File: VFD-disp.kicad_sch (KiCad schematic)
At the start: 97 parts, among them J1 USB_C_Receptacle_USB2.0_14P, J2 Conn_02x03_Odd_Even, J3 Jack-DC, J4 Conn_02x03_Odd_Even, J5 Conn_02x03_Odd_Even, J6 Conn_02x03_Odd_Even, Q1 NMOS, Q3 NMOS, SW1 SW_SPST, U1 ESP32-C6-WROOM-1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

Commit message: Reroute pcb
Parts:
- removed F3: Fuse, Fuse:Fuse_0805_2012Metric, symbol Device:Fuse
- removed J3: Jack-DC, Connector_BarrelJack:BarrelJack_Horizontal, symbol Connector:Jack-DC
- removed Q1, Q3: NMOS, Package_TO_SOT_SMD:TO-252-2, symbol Simulation_SPICE:NMOS
- added Q1, Q2: Q_NMOS_GDS, Package_TO_SOT_SMD:TO-263-2, symbol Transistor_FET:Q_NMOS_GDS
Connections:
- net GND: now also Q2.3 (S)
- net at R10.2, R11.1: now also Q2.1 (G)
- net at R4.1, U6.8 (CS): now also Q1.3 (S)
- net at D1.2 (A), L1.2: now also Q1.2 (D)
- net at U6.1 (EXT): now also Q1.1 (G)
- net at IVLM3-5/1.22 (F2): now also Q2.2 (D)

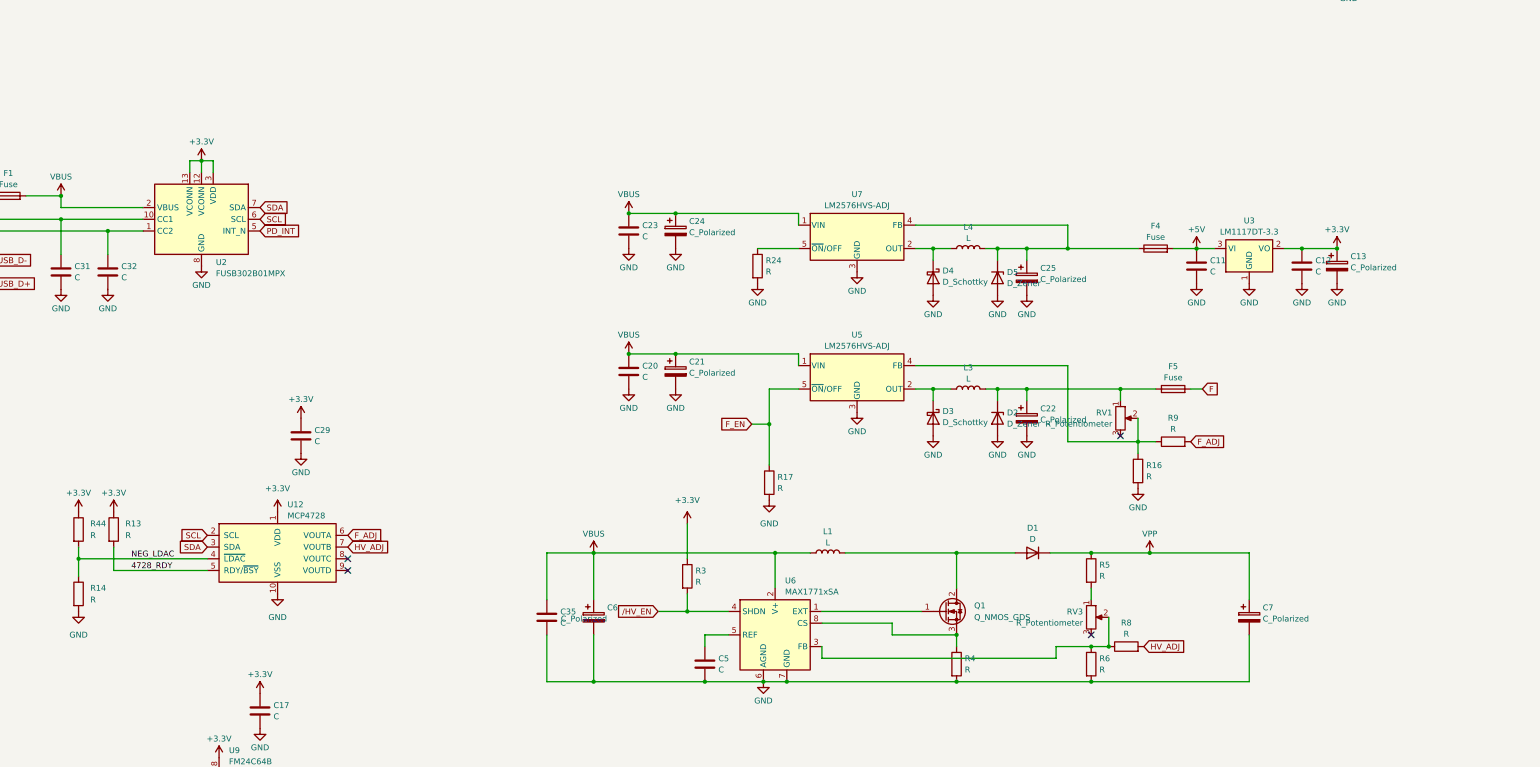
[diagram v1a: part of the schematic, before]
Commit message: Add chonky cermaics caps to be safe...
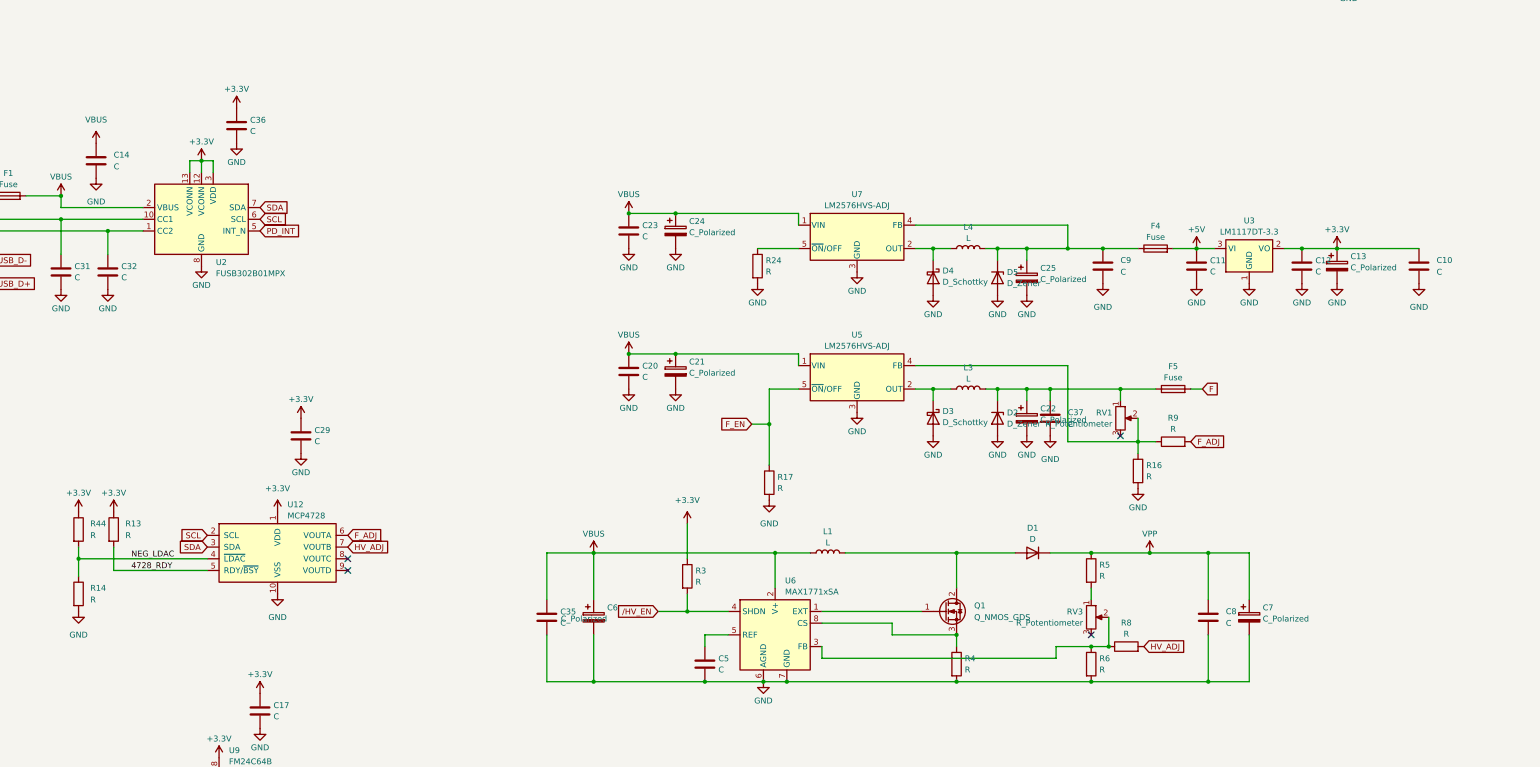
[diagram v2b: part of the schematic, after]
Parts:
- added C10, C14, C37, C8, C9: C, Capacitor_SMD:C_2220_5750Metric, symbol Device:C
- added C36: C, Capacitor_SMD:C_0805_2012Metric, symbol Device:C
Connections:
- net +3.3V: now also C10.1, C36.1
- net GND: now also C10.2, C14.2, C36.2, C37.2, C8.2, C9.2
- net VBUS: now also C14.1
- net VPP: now also C8.1
- net at C22.1, D2.1 (K), F5.1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: now also C37.1
- net at C25.1, D5.1 (K), F4.1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: now also C9.1

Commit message: Finish pcb
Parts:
- removed D5: D_Zener, Diode_SMD:D_MELF, symbol Device:D_Zener
- added C38, C39: 10uF, Capacitor_SMD:C_1206_3216Metric, symbol Device:C
- added C40, C41: C, Capacitor_SMD:C_0805_2012Metric, symbol Device:C
- added D6: BZV55B7V5, Diode_SMD:D_MiniMELF, symbol Diode:BZV55B7V5
- added Q3: Q_NPN_BEC, Package_TO_SOT_SMD:SOT-23, symbol Transistor_BJT:Q_NPN_BEC
- added R23, R27, R28, R29, R30: R, Resistor_SMD:R_0805_2012Metric, symbol Device:R
- added U13: TPS2116DRL, Package_TO_SOT_SMD:SOT-583-8, symbol Power_Management:TPS2116DRL
- added U14: KF50BDT, Package_TO_SOT_SMD:TO-252-2, symbol Regulator_Linear:KF50BDT
- added U8: USBLC6-2P6, Package_TO_SOT_SMD:SOT-666, symbol Power_Protection:USBLC6-2P6
- D1, D2, D3, D4: footprint Diode_SMD:D_MELF -> Diode_SMD:D_SMB
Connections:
- net +3.3V: now also R28.1, U8.5 (VBUS)
- net GND: now also C38.2, C39.2, C40.2, C41.2, Q3.2 (E), R27.2, R29.2, U13.1 (GND), U14.2 (GND), U8.2 (GND); no longer R24.2
- net USB_D+: now also U8.1 (I/O1); no longer U1.14 (GPIO13/USB_D+)
- net USB_D-: now also U8.3 (I/O2); no longer U1.13 (GPIO12/USB_D-)
- net VBUS: now also R24.1, C38.1, C40.1, R30.1, U14.1 (VI)
- net at C25.1, C9.1, L4.2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: now also R23.1, U13.3 (VIN1), U13.5 (MODE); no longer F4.1
- net at U7.5 (~{ON}/OFF): now also Q3.3 (C), R30.2; no longer R24.1
- net VBUS_ABOVE_TRESHOLD: now reaches U1.7 (MTDO/GPIO7)
- net VBUS_ABOVE_TRESHOLD: now also R28.2, U13.8 (ST)
- new net: C39.1, C41.1, U13.6 (VIN2), U14.3 (VO)
- new net: D6.2 (A), Q3.1 (B), R29.1
- new net: F4.1, U13.2 (VOUT), U13.7 (VOUT)
- new net: R23.2, R27.1, U13.4 (PR1)
- new net: D6.1 (K), R24.2
- new net PRE_USB_D+: U1.14 (GPIO13/USB_D+), U8.6 (I/O1)
- new net PRE_USB_D-: U1.13 (GPIO12/USB_D-), U8.4 (I/O2)
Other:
- moved on the sheet: C10, C11, C12, C13, C20, C21, C22, C35, C37, C5, C6, C7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

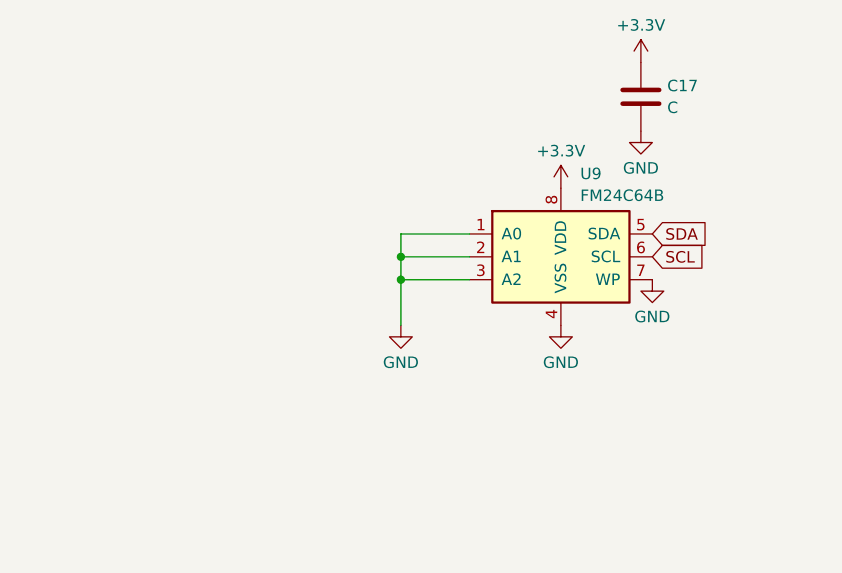
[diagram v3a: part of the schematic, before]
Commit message: Add mounting holes and some rework
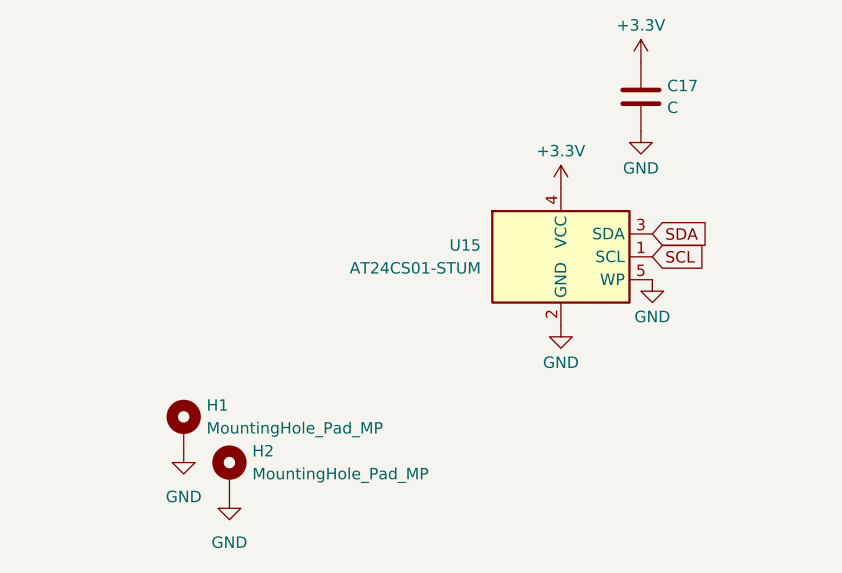
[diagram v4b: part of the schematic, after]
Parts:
- removed U9: FM24C64B, Package_SO:SOIC-8_3.9x4.9mm_P1.27mm, symbol Memory_NVRAM:FM24C64B
- added H1, H2: MountingHole_Pad_MP, MountingHole:MountingHole_2.2mm_M2_Pad_Via, symbol Mechanical:MountingHole_Pad_MP
- added U15: AT24CS01-STUM, Package_TO_SOT_SMD:SOT-23-5, symbol Memory_EEPROM:AT24CS01-STUM
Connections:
- net +3.3V: now also U15.4 (VCC)
- net GND: now also H1.MP, H2.MP, U15.2 (GND), U15.5 (WP)
- net SCL: now also U15.1 (SCL)
- net SDA: now also U15.3 (SDA)

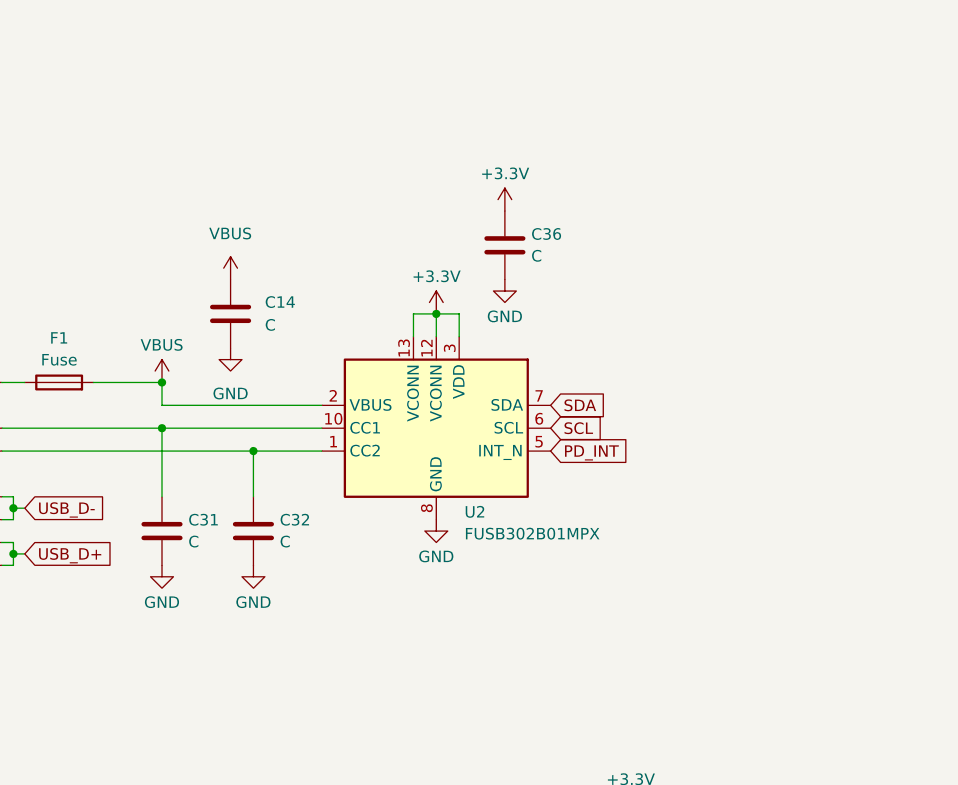
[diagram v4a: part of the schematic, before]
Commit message: Add CC lines pull down
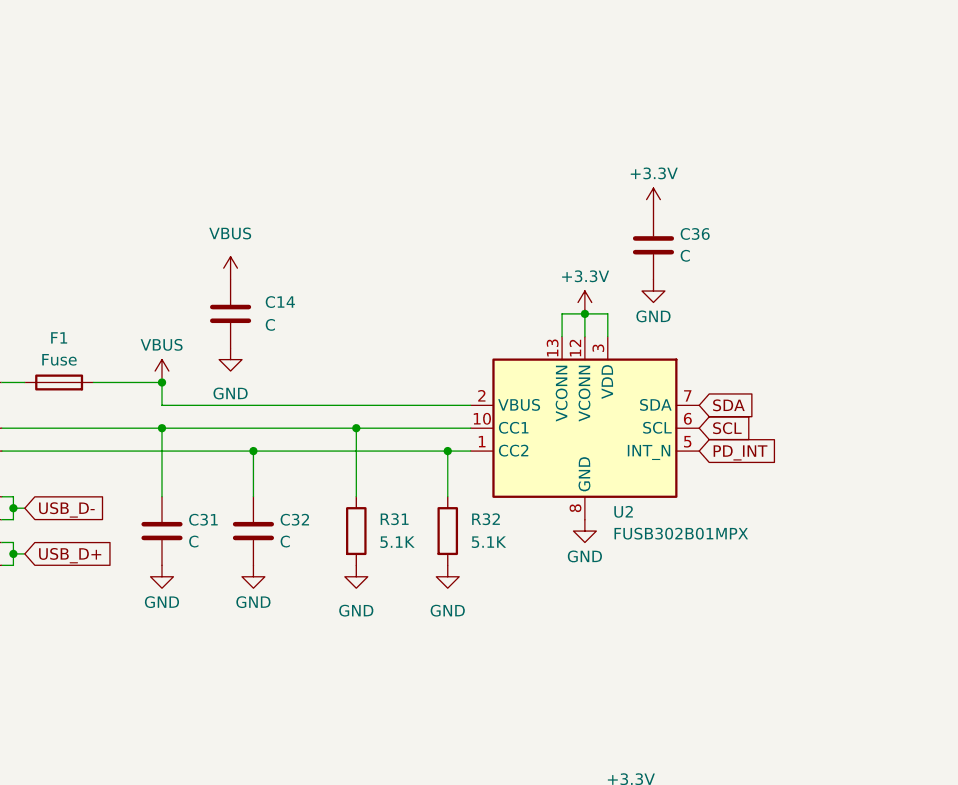
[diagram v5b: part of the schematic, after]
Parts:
- added R31, R32: 5.1K, Resistor_SMD:R_0805_2012Metric, symbol Device:R
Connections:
- net GND: now also R31.2, R32.2
- net at C31.1, J1.A5 (CC1), U2.10 (CC1)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: now also R31.1
- net at C32.1, J1.B5 (CC2), U2.1 (CC2)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: now also R32.1
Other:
- moved on the sheet: C36, U2

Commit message: Fix screw connections
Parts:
- removed H1, H2: MountingHole_Pad_MP, MountingHole:MountingHole_2.2mm_M2_Pad_Via, symbol Mechanical:MountingHole_Pad_MP
- added H1, H2: MountingHole_Pad, MountingHole:MountingHole_2.2mm_M2_Pad_Via, symbol Mechanical:MountingHole_Pad
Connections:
- net GND: now also H1.1, H2.1
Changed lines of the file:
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@@
 	)
 	(symbol
-		(lib_id "Mechanical:MountingHole_Pad_MP")
-		(at 69.85 377.19 0)
-		(unit 1)
-		(exclude_from_sim no)
-		(in_bom no)
-		(on_board yes)
-		(dnp no)
-		(fields_autoplaced yes)
-		(property "Reference" "H2"
-			(at 72.39 374.6499 0)
-			(effects
-				(font
-					(size 1.27 1.27)
-				)
-				(justify left)
-			)
-		)
-		(property "Value" "MountingHole_Pad_MP"
-			(at 72.39 377.1899 0)
-			(effects
-				(font
-					(size 1.27 1.27)
-				)
-				(justify left)
-			)
-		)
-		(property "Footprint" "MountingHole:MountingHole_2.2mm_M2_Pad_Via"
-			(at 69.85 377.19 0)
-			(effects
-				(font
-					(size 1.27 1.27)
-				)
-				(hide yes)
-			)
-		)
-		(property "Datasheet" "~"
-			(at 69.85 377.19 0)
-			(effects
-				(font
-					(size 1.27 1.27)
-				)
-				(hide yes)
-			)
-		)
-		(property "Description" "Mounting Hole with connection as pad named MP"
-			(at 69.85 377.19 0)
-			(effects
-				(font
-					(size 1.27 1.27)
-				)
-				(hide yes)
-			)
-		)
-		(pin "MP"
-		)
-		(instances
-			(project "VFD-disp"
-				(path "/cae6bc37-1dab-478a-ae03-a930606a6e90"
-					(reference "H2")
-					(unit 1)
-				)
-			)
-		)
-	)
-	(symbol
 		(lib_id "Device:R")
 		(at 226.06 322.58 0)
@@
 	)
 	(symbol
-		(lib_id "Mechanical:MountingHole_Pad_MP")
-		(at 64.77 372.11 0)
-		(unit 1)
-		(exclude_from_sim no)
-		(in_bom no)
-		(on_board yes)
-		(dnp no)
-		(fields_autoplaced yes)
-		(property "Reference" "H1"
-			(at 67.31 369.5699 0)
-			(effects
-				(font
-					(size 1.27 1.27)
-				)
-				(justify left)
-			)
-		)
-		(property "Value" "MountingHole_Pad_MP"
-			(at 67.31 372.1099 0)
-			(effects
-				(font
-					(size 1.27 1.27)
-				)
-				(justify left)
-			)
-		)
-		(property "Footprint" "MountingHole:MountingHole_2.2mm_M2_Pad_Via"
-			(at 64.77 372.11 0)
-			(effects
-				(font
-					(size 1.27 1.27)
-				)
-				(hide yes)
-			)
-		)
-		(property "Datasheet" "~"
-			(at 64.77 372.11 0)
-			(effects
-				(font
-					(size 1.27 1.27)
-				)
-				(hide yes)
-			)
-		)
-		(property "Description" "Mounting Hole with connection as pad named MP"
-			(at 64.77 372.11 0)
-			(effects
-				(font
-					(size 1.27 1.27)
-				)
-				(hide yes)
-			)
-		)
-		(pin "MP"
-		)
-		(instances
-			(project ""
-				(path "/cae6bc37-1dab-478a-ae03-a930606a6e90"
-					(reference "H1")
-					(unit 1)
-				)
-			)
-		)
-	)
-	(symbol
 		(lib_id "power:GND")
 		(at 104.14 243.84 0)
@@
 	)
 	(symbol
+		(lib_id "Mechanical:MountingHole_Pad")
+		(at 69.85 377.19 0)
+		(unit 1)
+		(exclude_from_sim no)
+		(in_bom no)
+		(on_board yes)
+		(dnp no)
+		(fields_autoplaced yes)
+		(property "Reference" "H2"
+			(at 72.39 374.6499 0)
+			(effects
+				(font
+					(size 1.27 1.27)
+				)
+				(justify left)
+			)
+		)
+		(property "Value" "MountingHole_Pad"
+			(at 72.39 377.1899 0)
+			(effects
+				(font
+					(size 1.27 1.27)
+				)
+				(justify left)
+			)
+		)
+		(property "Footprint" "MountingHole:MountingHole_2.2mm_M2_Pad_Via"
+			(at 69.85 377.19 0)
+			(effects
+				(font
+					(size 1.27 1.27)
+				)
+				(hide yes)
+			)
+		)
+		(property "Datasheet" "~"
+			(at 69.85 377.19 0)
+			(effects
+				(font
+					(size 1.27 1.27)
+				)
+				(hide yes)
+			)
+		)
+		(property "Description" "Mounting Hole with connection"
+			(at 69.85 377.19 0)
+			(effects
+				(font
+					(size 1.27 1.27)
+				)
+				(hide yes)
+			)
+		)
+		(pin "1"
+		)
+		(instances
+			(project "VFD-disp"
+				(path "/cae6bc37-1dab-478a-ae03-a930606a6e90"
+					(reference "H2")
+					(unit 1)
+				)
+			)
+		)
+	)
+	(symbol
 		(lib_id "Device:C_Polarized")
 		(at 467.36 158.75 0)
@@
 					(unit 1)
 				)
+			)
+		)
+	)
+	(symbol
+		(lib_id "Mechanical:MountingHole_Pad")
+		(at 64.77 372.11 0)
+		(unit 1)
+		(exclude_from_sim no)
+		(in_bom no)
+		(on_board yes)
+		(dnp no)
+		(fields_autoplaced yes)
+		(property "Reference" "H1"
+			(at 67.31 369.5699 0)
+			(effects
+				(font
+					(size 1.27 1.27)
+				)
+				(justify left)
+			)
+		)
+		(property "Value" "MountingHole_Pad"
+			(at 67.31 372.1099 0)
+			(effects
+				(font
+					(size 1.27 1.27)
+				)
+				(justify left)
+			)
+		)
+		(property "Footprint" "MountingHole:MountingHole_2.2mm_M2_Pad_Via"
+			(at 64.77 372.11 0)
+			(effects
+				(font
+					(size 1.27 1.27)
+				)
+				(hide yes)
+			)
+		)
+		(property "Datasheet" "~"
+			(at 64.77 372.11 0)
+			(effects
+				(font
+					(size 1.27 1.27)
+				)
+				(hide yes)
+			)
+		)
+		(property "Description" "Mounting Hole with connection"
+			(at 64.77 372.11 0)
+			(effects
+				(font
+					(size 1.27 1.27)
+				)
+				(hide yes)
+			)
+		)
+		(pin "1"
+		)
+		(instances
+			(project ""
+				(path "/cae6bc37-1dab-478a-ae03-a930606a6e90"
+					(reference "H1")
+					(unit 1)
+				)

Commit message: Fix silkscreen and plot gerber
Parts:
- IVLM3-5/1: value ~ -> (none)
